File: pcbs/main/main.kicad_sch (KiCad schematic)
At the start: 1 part, among them J1 JST_XH_B3B

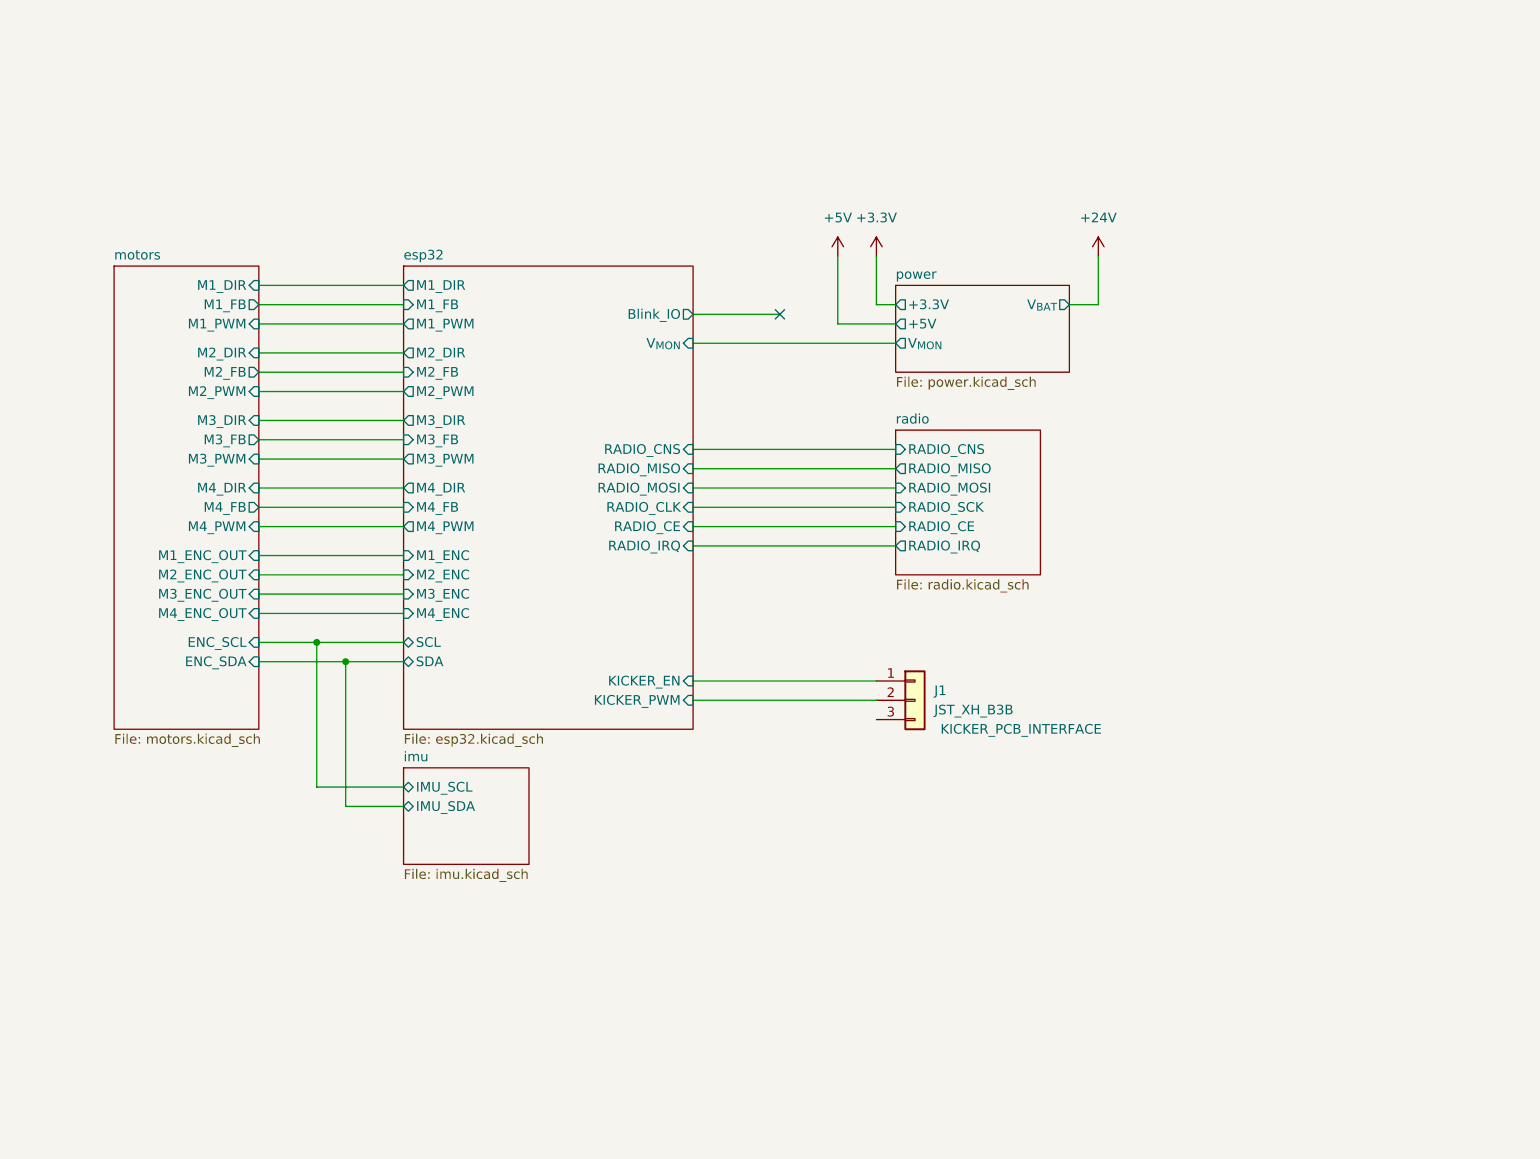
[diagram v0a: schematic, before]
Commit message: Add TOF symbol and refactor the schematic to be cleaner
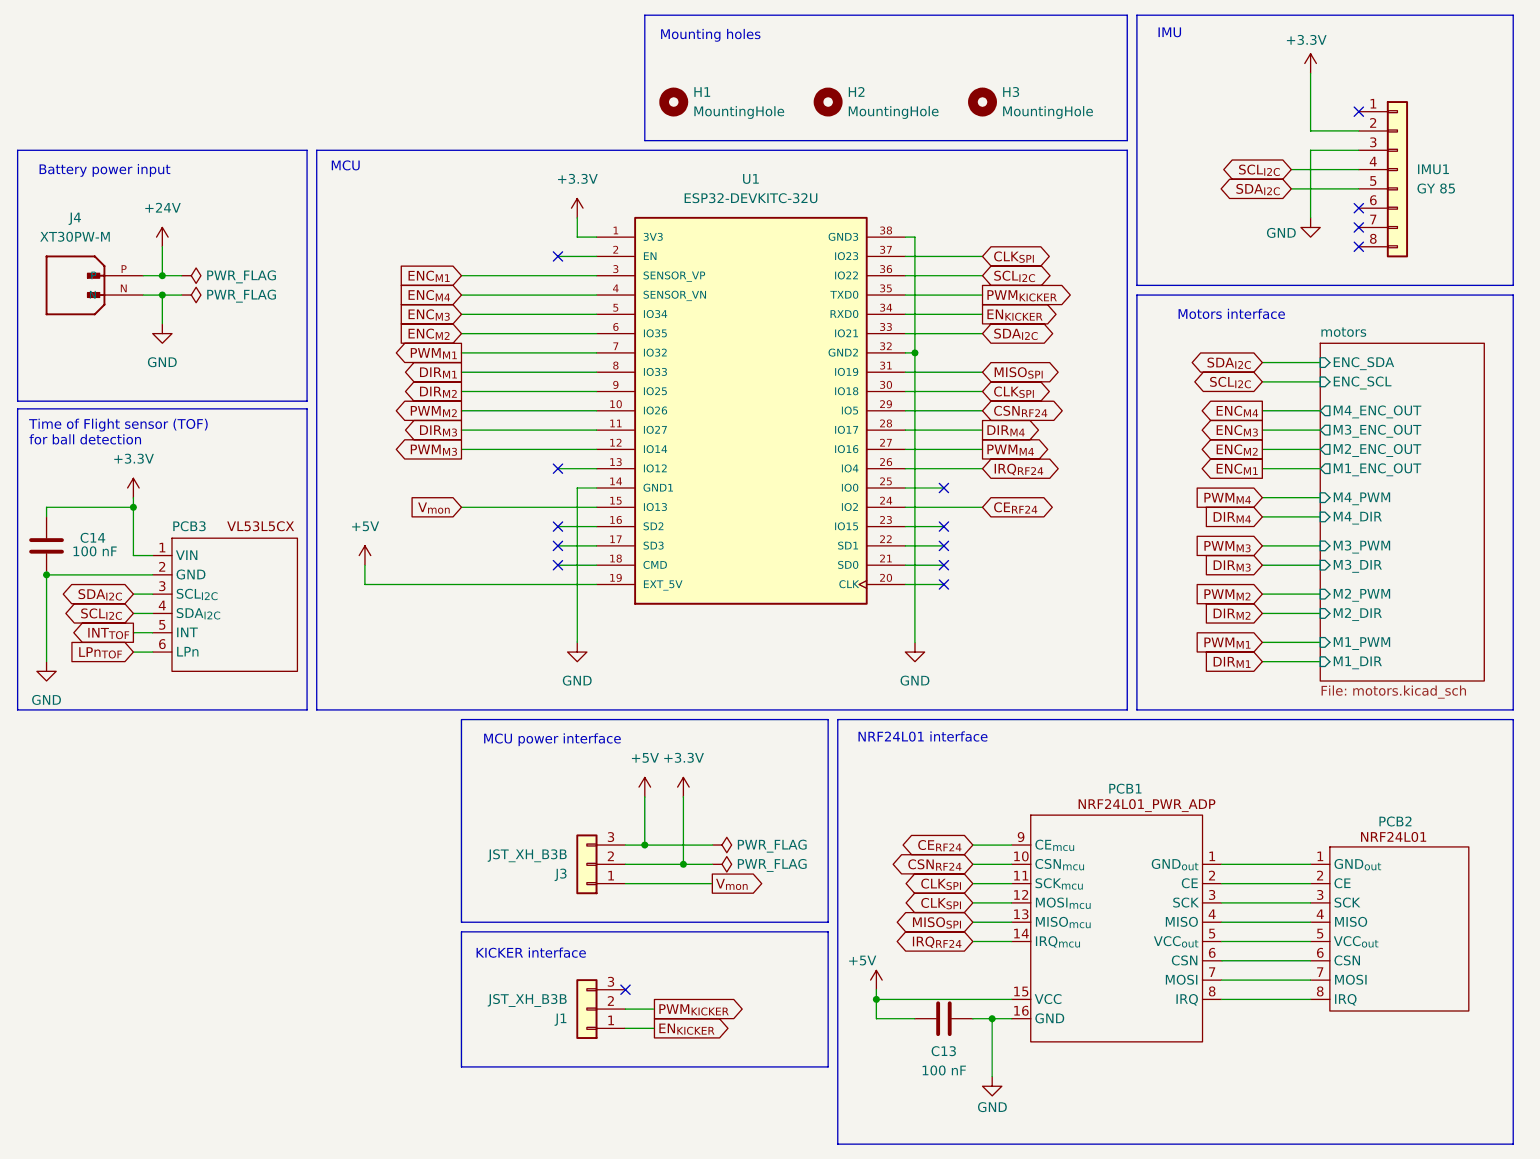
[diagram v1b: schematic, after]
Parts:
- added C13, C14: 100 nF, Capacitor_THT:C_Disc_D5.0mm_W2.5mm_P2.50mm, symbol Device:C
- added H1, H2, H3: MountingHole, MountingHole:MountingHole_2.5mm_Pad_TopBottom, symbol Mechanical:MountingHole
- added IMU1: GY 85, Oxebots:GY-085, symbol Connector_Generic:Conn_01x08
- added J3: JST_XH_B3B, Connector_JST:JST_XH_B3B-XH-A_1x03_P2.50mm_Vertical, symbol Connector_Generic:Conn_01x03
- added J4: XT30PW-M, Oxebots:AMASS_XT30PW-M, symbol XT30PW-M:XT30PW-M
- added PCB1: (no value), Oxebots:NRF24L01_PWR_ADP, symbol oxebots:NRF24L01_PWR_ADP
- added PCB2: (no value), Oxebots:NRF24L01, symbol oxebots:NRF24L01
- added PCB3: (no value), symbol oxebots:VL53L5CX
- added U1: ESP32-DEVKITC-32U, Oxebots:MODULE_ESP32-DEVKITC-32U, symbol ESP32-DEVKITC-32U:ESP32-DEVKITC-32U
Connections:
- net +24V: now also J4.P
- net +3.3V: now also C14.2, IMU1.2 (Pin_2), J3.2 (Pin_2), PCB3.1 (VIN), U1.1 (3V3)
- net +5V: now also C13.1, J3.3 (Pin_3), PCB1.15 (VCC), U1.19 (EXT_5V)
- net esp32/KICKER_EN renamed EN_{KICKER}
- net EN_{KICKER}: now also U1.34 (RXD0)
- net esp32/KICKER_PWM renamed PWM_{KICKER}
- net PWM_{KICKER}: now also U1.35 (TXD0)
- new net: PCB1.1 (GND_{out}), PCB2.1 (GND_{out})
- new net: PCB1.2 (CE), PCB2.2 (CE)
- new net: PCB1.3 (SCK), PCB2.3 (SCK)
- new net: PCB1.4 (MISO), PCB2.4 (MISO)
- new net: PCB1.5 (VCC_{out}), PCB2.5 (VCC_{out})
- new net: PCB1.6 (CSN), PCB2.6 (CSN)
- new net: PCB1.7 (MOSI), PCB2.7 (MOSI)
- new net: PCB1.8 (IRQ), PCB2.8 (IRQ)
- new net CE_{RF24}: PCB1.9 (CE_{mcu}), U1.24 (IO2)
- new net CLK_{SPI}: PCB1.11 (SCK_{mcu}), PCB1.12 (MOSI_{mcu}), U1.30 (IO18), U1.37 (IO23)
- new net CSN_{RF24}: PCB1.10 (CSN_{mcu}), U1.29 (IO5)
- new net DIR_{M1}: U1.8 (IO33)
- new net DIR_{M2}: U1.9 (IO25)
- new net DIR_{M3}: U1.11 (IO27)
- new net DIR_{M4}: U1.28 (IO17)
- new net ENC_{M1}: U1.3 (SENSOR_VP)
- new net ENC_{M2}: U1.6 (IO35)
- new net ENC_{M3}: U1.5 (IO34)
- new net ENC_{M4}: U1.4 (SENSOR_VN)
- new net GND: C13.2, C14.1, IMU1.3 (Pin_3), J4.N, PCB1.16 (GND), PCB3.2 (GND), U1.14 (GND1), U1.32 (GND2), U1.38 (GND3)
- new net INT_{TOF}: PCB3.5 (INT)
- new net IRQ_{RF24}: PCB1.14 (IRQ_{mcu}), U1.26 (IO4)
- new net LPn_{TOF}: PCB3.6 (LPn)
- new net MISO_{SPI}: PCB1.13 (MISO_{mcu}), U1.31 (IO19)
- new net PWM_{M1}: U1.7 (IO32)
- new net PWM_{M2}: U1.10 (IO26)
- new net PWM_{M3}: U1.12 (IO14)
- new net PWM_{M4}: U1.27 (IO16)
- new net SCL_{I2C}: IMU1.4 (Pin_4), PCB3.4 (SDA_{I2C}), U1.36 (IO22)
- new net SDA_{I2C}: IMU1.5 (Pin_5), PCB3.3 (SCL_{I2C}), U1.33 (IO21)
- new net V_{mon}: J3.1 (Pin_1), U1.15 (IO13)
- no-connect marks 1 -> 15
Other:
- removed sheet esp32
- removed sheet imu
- removed sheet power
- removed sheet radio
- sheet motors ports: added none; removed M1_FB, M2_FB, M3_FB, M4_FB
- note added: "Battery power input"
- note added: "IMU"
- note added: "KICKER interface"
- note added: "MCU"
- note added: "MCU power interface"
- note added: "Motors interface"
- note added: "Mounting holes"
- note added: "NRF24L01 interface"
- note added: "Time of Flight sensor (TOF) for ball detection"
- moved on the sheet: J1

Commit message: Update footprint for TOF and encoders
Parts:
- PCB3: footprint (none) -> Connector_JST:JST_XH_B6B-XH-A_1x06_P2.50mm_Vertical
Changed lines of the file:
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@@
 			)
 		)
-		(property "Footprint" ""
+		(property "Footprint" "Connector_JST:JST_XH_B6B-XH-A_1x06_P2.50mm_Vertical"
 			(at 116.84 93.98 0)
 			(hide yes)
